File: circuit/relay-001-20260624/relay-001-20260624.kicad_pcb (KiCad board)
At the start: 2 copper layers, 169 x 126.3 mm, 15 parts, among them J1 Conn_01x03_Pin, J10 Conn_01x02_Pin, J11 Conn_01x02_Pin, J12 Conn_01x02_Pin, J13 Conn_01x02_Pin, J14 Conn_01x02_Pin, J15 Conn_01x02_Pin, J2 Conn_02x05_Odd_Even, J3 Conn_02x08_Odd_Even, J4 Conn_02x09_Odd_Even, J5 Conn_01x02_Pin, J6 Conn_01x02_Pin, J7 Conn_01x02_Pin, J8 Conn_01x02_Pin, J9 Conn_01x02_Pin

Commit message: Update 供給基板のボード図を進めた
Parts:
- moved J14 184.3 mm to (185.2, 35.6), turned to -34.8 degrees
- moved J13 171.7 mm to (202.6, 123.8), turned to -124.8 degrees
- moved J9 146.4 mm to (177.4, 104.2), turned to -90 degrees
- moved J11 111.6 mm to (112.6, 37.0), turned to 34.8 degrees
- moved J7 86.1 mm to (121.4, 90.4), turned to 90 degrees
- moved J6 74.9 mm to (114.8, 103.4), turned to 90 degrees
- moved J1 71.9 mm to (123.8, 98.9)
- moved J15 69.6 mm to (80.3, 95.2), turned to -90 degrees
- moved J12 67.6 mm to (98.4, 125.7), turned to 124.8 degrees
- moved J8 51.6 mm to (186.3, 107.9)
- moved J4 16.8 mm to (205.0, 76.1), turned to -90 degrees
- moved J5 8.42 mm to (114.8, 77.4)
- moved J10 3.67 mm to (135.8, 119.0)
- moved J2 3.67 mm to (144.8, 62.7)
- moved J3 3.67 mm to (150.3, 119.4)
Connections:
- J10 pad 1: VCC -> GND
- J10 pad 2: GND -> VCC
- J2 pad 1: GND -> EN_{Boost}
- J2 pad 10: +3.3V -> GND
- J2 pad 2: EN_{Boost} -> GND
- J2 pad 3: EN_{Dribbler-Front} -> Kick_{Chip}
- J2 pad 4: Kick_{Chip} -> EN_{Dribbler-Front}
- J2 pad 5: PH_{Dribbler-Front} -> VCC
- J2 pad 6: VCC -> PH_{Dribbler-Front}
- J2 pad 7: BallCatch_{Front} -> Kick_{Stroke}
- J2 pad 8: Kick_{Stroke} -> BallCatch_{Front}
- J2 pad 9: GND -> +3.3V
- J3 pad 1: Motor_{OUT1-1} -> BallCatch_{Back}
- J3 pad 10: Motor2_{PWM} -> Motor_{OUT2-2}
- J3 pad 11: Motor_{OUT3-2} -> Motor_{EN}
- J3 pad 12: Motor3_{PWM} -> Motor_{OUT2-1}
- J3 pad 13: Motor_{OUT4-1} -> +3.3V
- J3 pad 14: Motor4_{PWM} -> Motor_{OUT1-2}
- J3 pad 15: Motor_{OUT4-2} -> GND
- J3 pad 16: BallCatch_{Back} -> Motor_{OUT1-1}
- J3 pad 2: +3.3V -> Motor_{OUT4-2}
- J3 pad 3: Motor_{OUT1-2} -> Motor4_{PWM}
- J3 pad 4: GND -> Motor_{OUT4-1}
- J3 pad 5: Motor_{OUT2-1} -> Motor3_{PWM}
- J3 pad 6: Motor_{EN} -> Motor_{OUT3-2}
- J3 pad 7: Motor_{OUT2-2} -> Motor2_{PWM}
- J3 pad 8: Motor1_{PWM} -> Motor_{OUT3-1}
- J3 pad 9: Motor_{OUT3-1} -> Motor1_{PWM}
- J5 pad 1: +5V_{Line} -> GND
- J5 pad 2: GND -> +5V_{Line}
- J6 pad 1: VCC -> GND
- J6 pad 2: GND -> VCC
- J7 pad 1: +5V -> +3.3V
- J7 pad 2: +3.3V -> +5V
- J8 pad 1: +5V_{Line} -> GND
- J8 pad 2: GND -> +5V_{Line}
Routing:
- net +3.3V: track 0.00 -> 199.4 mm, vias 0 -> 1
- net VCC: track 0.00 -> 182.2 mm
- net Motor_{OUT1-2}: track 0.00 -> 139.2 mm, vias 0 -> 2
- net Motor_{OUT1-1}: track 0.00 -> 129.6 mm, vias 0 -> 2
- net Motor_{OUT4-1}: track 0.00 -> 117.5 mm, vias 0 -> 1
- net Motor3_{PWM}: track 0.00 -> 117.1 mm, vias 0 -> 1
- net Motor2_{PWM}: track 0.00 -> 113.9 mm
- net Motor1_{PWM}: track 0.00 -> 110.5 mm
- net Motor_{EN}: track 0.00 -> 108.4 mm
- net Motor_{OUT4-2}: track 0.00 -> 107.8 mm, vias 0 -> 1
- net +5V_{Line}: track 0.00 -> 88.7 mm
- net +5V: track 0.00 -> 78.0 mm
- net Motor_{OUT2-1}: track 0.00 -> 72.5 mm
- net Motor_{OUT2-2}: track 0.00 -> 70.5 mm
- net Motor_{OUT3-2}: track 0.00 -> 53.0 mm
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- added copper zone on F.Cu, net VCC
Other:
- outline, holes or cut-outs redrawn

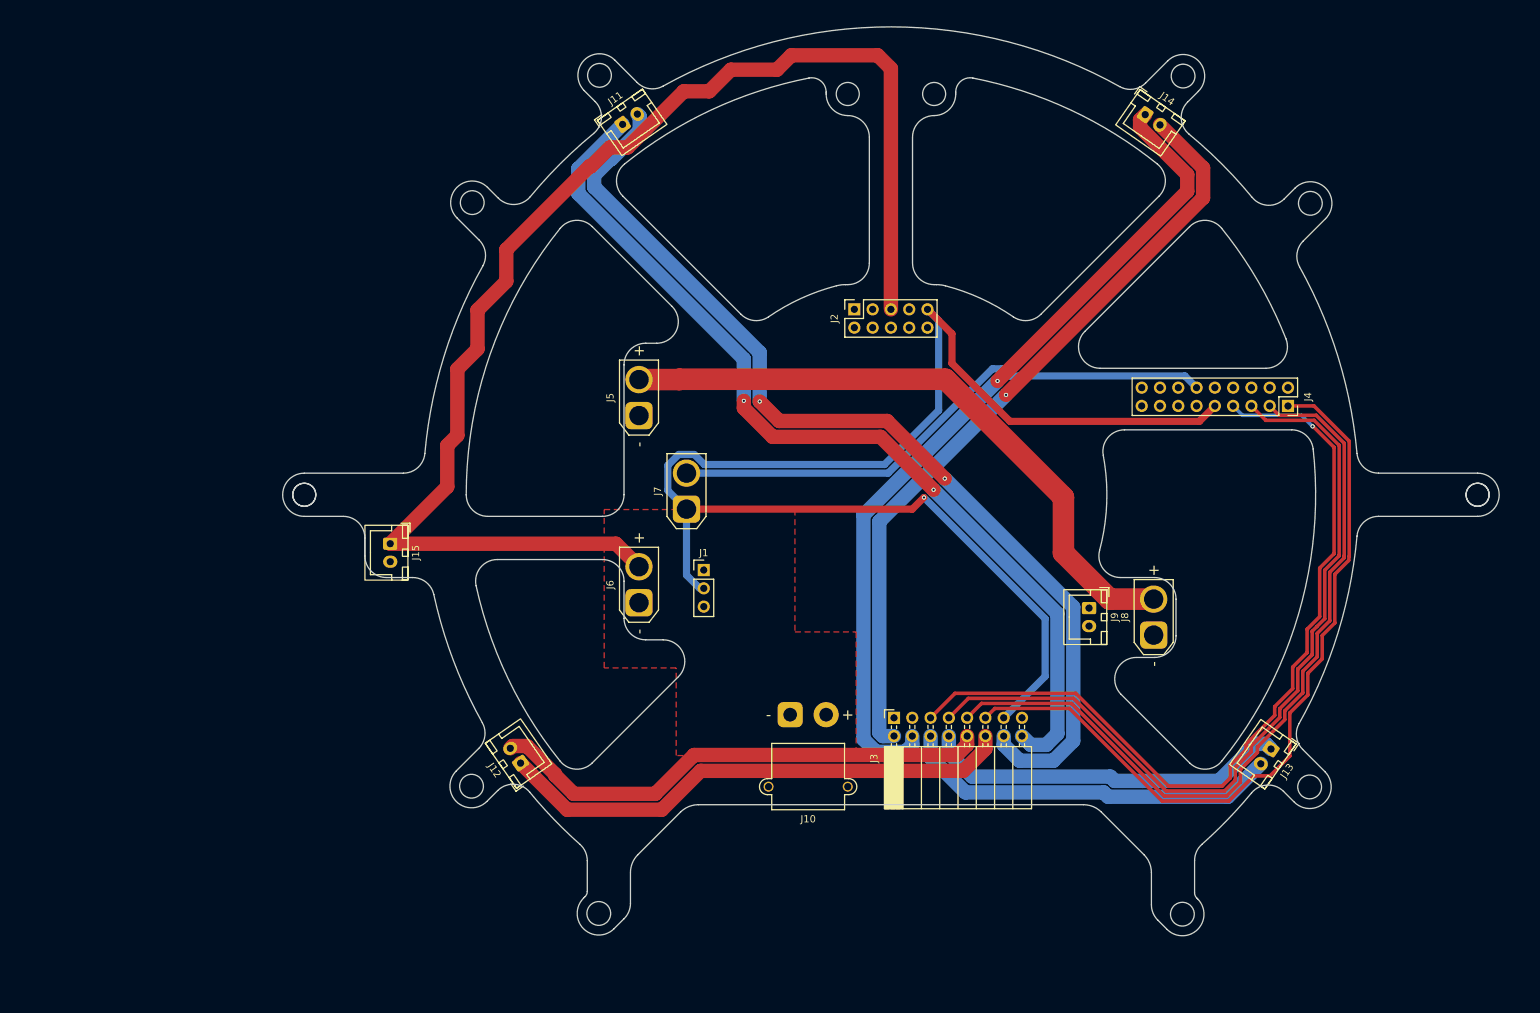
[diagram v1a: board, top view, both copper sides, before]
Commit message: Update 供給基板のDXFとボード図を更新
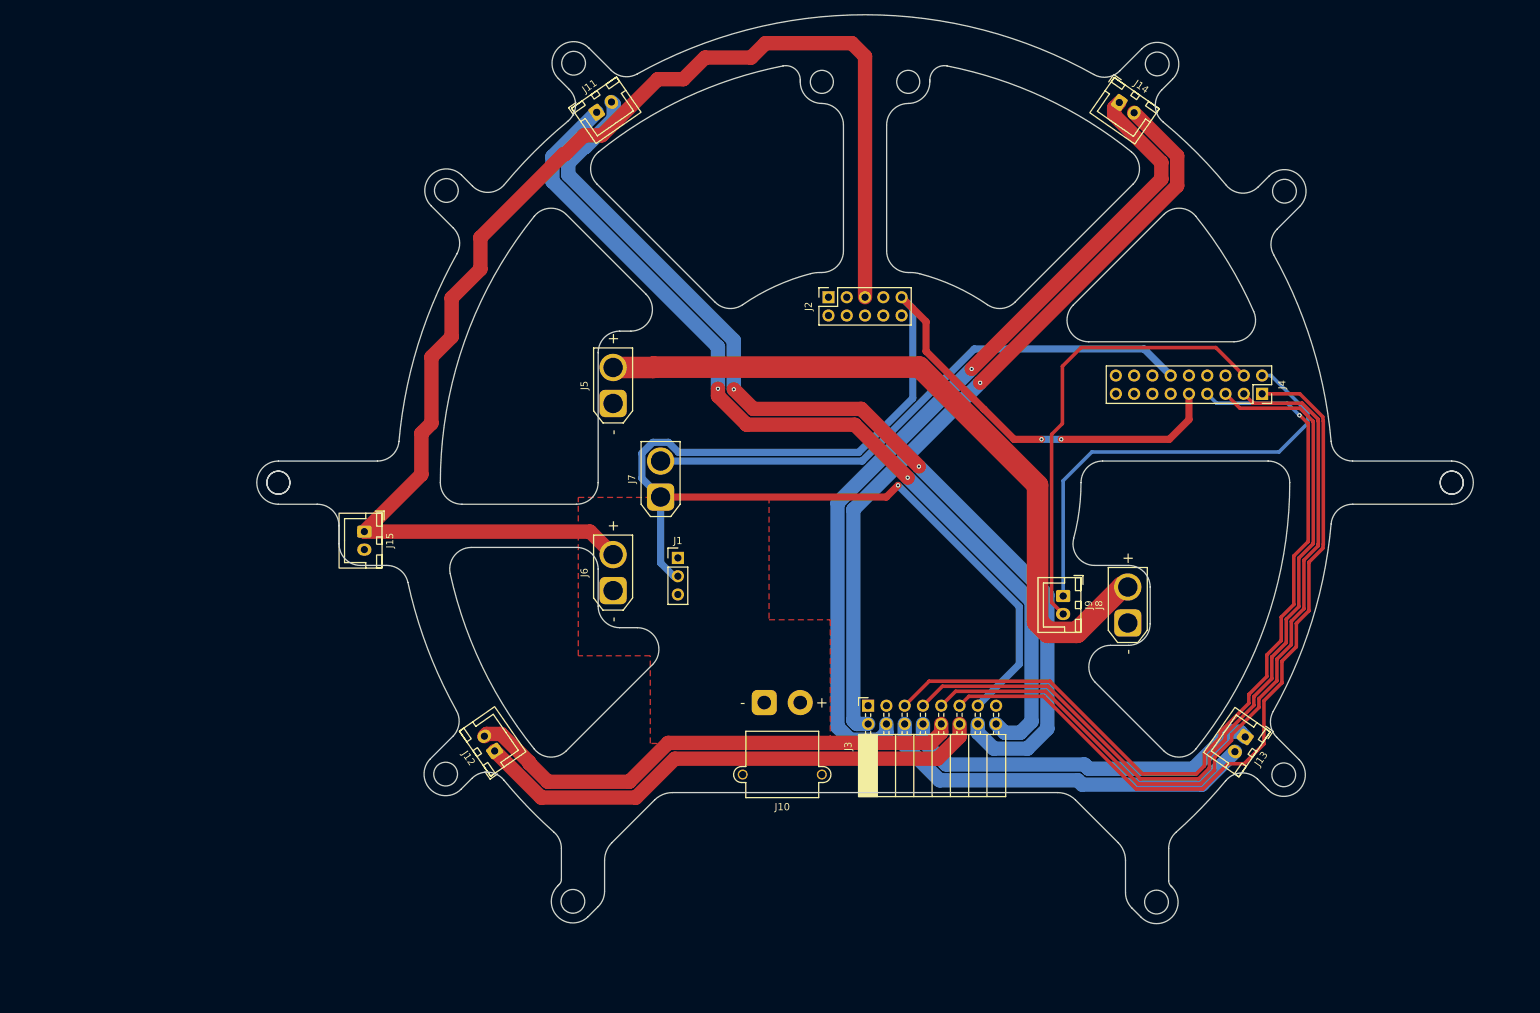
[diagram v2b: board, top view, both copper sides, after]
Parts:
- moved J1 3.97 mm to (120.2, 97.2)
- moved J3 3.97 mm to (146.7, 117.7)
- moved J5 3.97 mm to (111.2, 75.8)
- moved J6 3.97 mm to (111.2, 101.8)
- moved J2 3.97 mm to (141.2, 61.0)
- moved J10 3.97 mm to (132.2, 117.3)
- moved J12 3.97 mm to (94.8, 124.0)
- moved J13 3.97 mm to (199.0, 122.1)
- moved J14 3.97 mm to (181.6, 34.0)
- moved J15 3.97 mm to (76.7, 93.6)
- moved J9 3.97 mm to (173.8, 102.5)
- moved J11 3.97 mm to (109.0, 35.3)
- moved J7 3.97 mm to (117.8, 88.8)
- moved J4 3.97 mm to (201.4, 74.4)
- moved J8 3.97 mm to (182.7, 106.3)
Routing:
- net RX_{teensy}-TX_{Arduino}-5V: track 0.00 -> 63.6 mm
- net TX_{teensy}-RX_{Arduino}-5V: track 0.00 -> 63.3 mm
- net +5V_{Line}: track 88.7 -> 100.5 mm
- net +3.3V: track 199.4 -> 205.0 mm, vias 1 -> 3
- net Motor1_{PWM}: track 110.5 -> 111.4 mm
- net Motor3_{PWM}: track 117.1 -> 118.1 mm
- net Motor2_{PWM}: track 113.9 -> 114.8 mm
- net Motor_{EN}: track 108.4 -> 109.3 mm
- net +5V: track 78.0 -> 78.8 mm
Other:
- outline, holes or cut-outs redrawn

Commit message: Update 供給基板のボード図を更新
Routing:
- net BallCatch_{Front}: track 0.00 -> 53.2 mm, vias 0 -> 3
- net +3.3V: track 205.0 -> 198.6 mm, vias 3 -> 4

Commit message: Update 供給基板のボード図を更新
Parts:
- moved J8 13.3 mm to (172.3, 114.5)
- moved J7 13.3 mm to (107.4, 97.0)
- moved J11 13.3 mm to (98.5, 43.6)
- moved J1 13.3 mm to (109.8, 105.5)
- moved J10 13.3 mm to (121.8, 125.6)
- moved J12 13.3 mm to (84.3, 132.3)
- moved J3 13.3 mm to (136.2, 126.0)
- moved J4 13.3 mm to (190.9, 82.7)
- moved J5 13.3 mm to (100.8, 84.0)
- moved J6 13.3 mm to (100.8, 110.0)
- moved J9 13.3 mm to (163.3, 110.8)
- moved J14 13.3 mm to (171.1, 42.2)
- moved J2 13.3 mm to (130.7, 69.3)
- moved J15 13.3 mm to (66.2, 101.8)
- moved J13 13.3 mm to (188.6, 130.4)
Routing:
- net BallCatch_{Back}: track 0.00 -> 88.2 mm, vias 0 -> 4
- net Motor4_{PWM}: track 0.00 -> 84.7 mm, vias 0 -> 4
- net Dribbler_{Back}: track 0.00 -> 77.3 mm, vias 0 -> 2
- net EN_{Dribbler-Front}: track 0.00 -> 56.7 mm, vias 0 -> 1
- net PH_{Dribbler-Front}: track 0.00 -> 56.7 mm, vias 0 -> 1
- net EN_{Boost}: track 0.00 -> 56.0 mm, vias 0 -> 1
- net Kick_{Chip}: track 0.00 -> 46.4 mm, vias 0 -> 1
- net Kick_{Stroke}: track 0.00 -> 41.5 mm, vias 0 -> 1
- net +5V: track 78.8 -> 83.4 mm
- net BallCatch_{Front}: track 53.2 -> 54.6 mm
- net RX_{teensy}-TX_{Arduino}-5V: track 63.6 -> 64.7 mm
- added copper zone on F.Cu, net GND

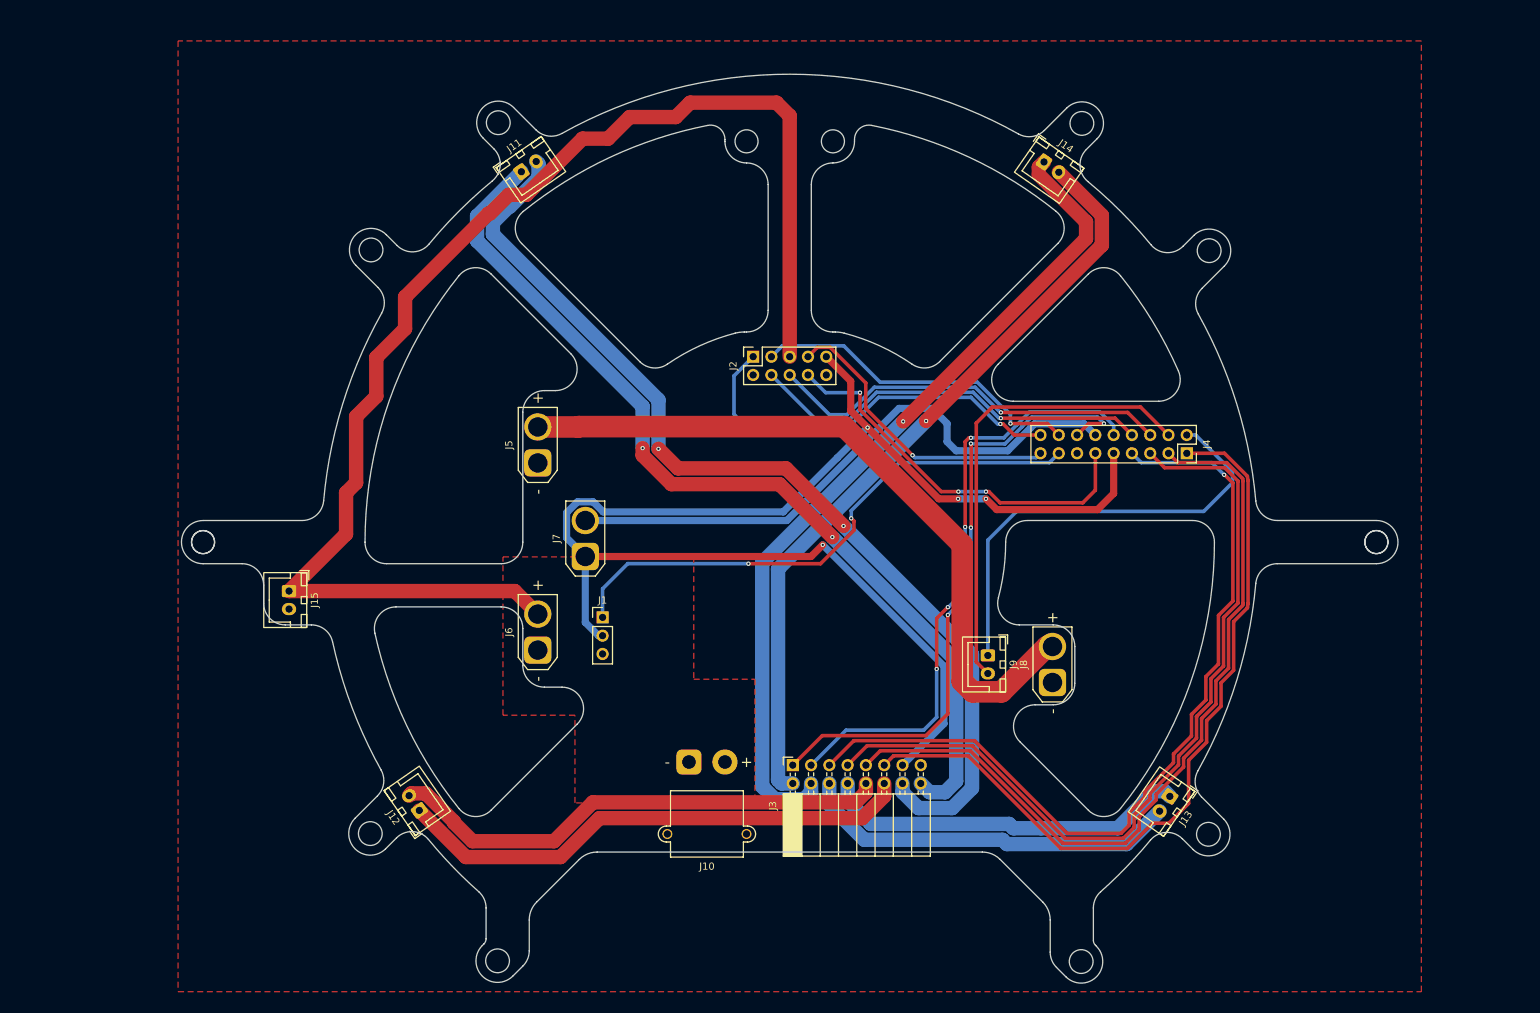
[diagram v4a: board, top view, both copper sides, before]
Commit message: Update 供給基板のボード図、キッカー基板の発注ファイルを更新
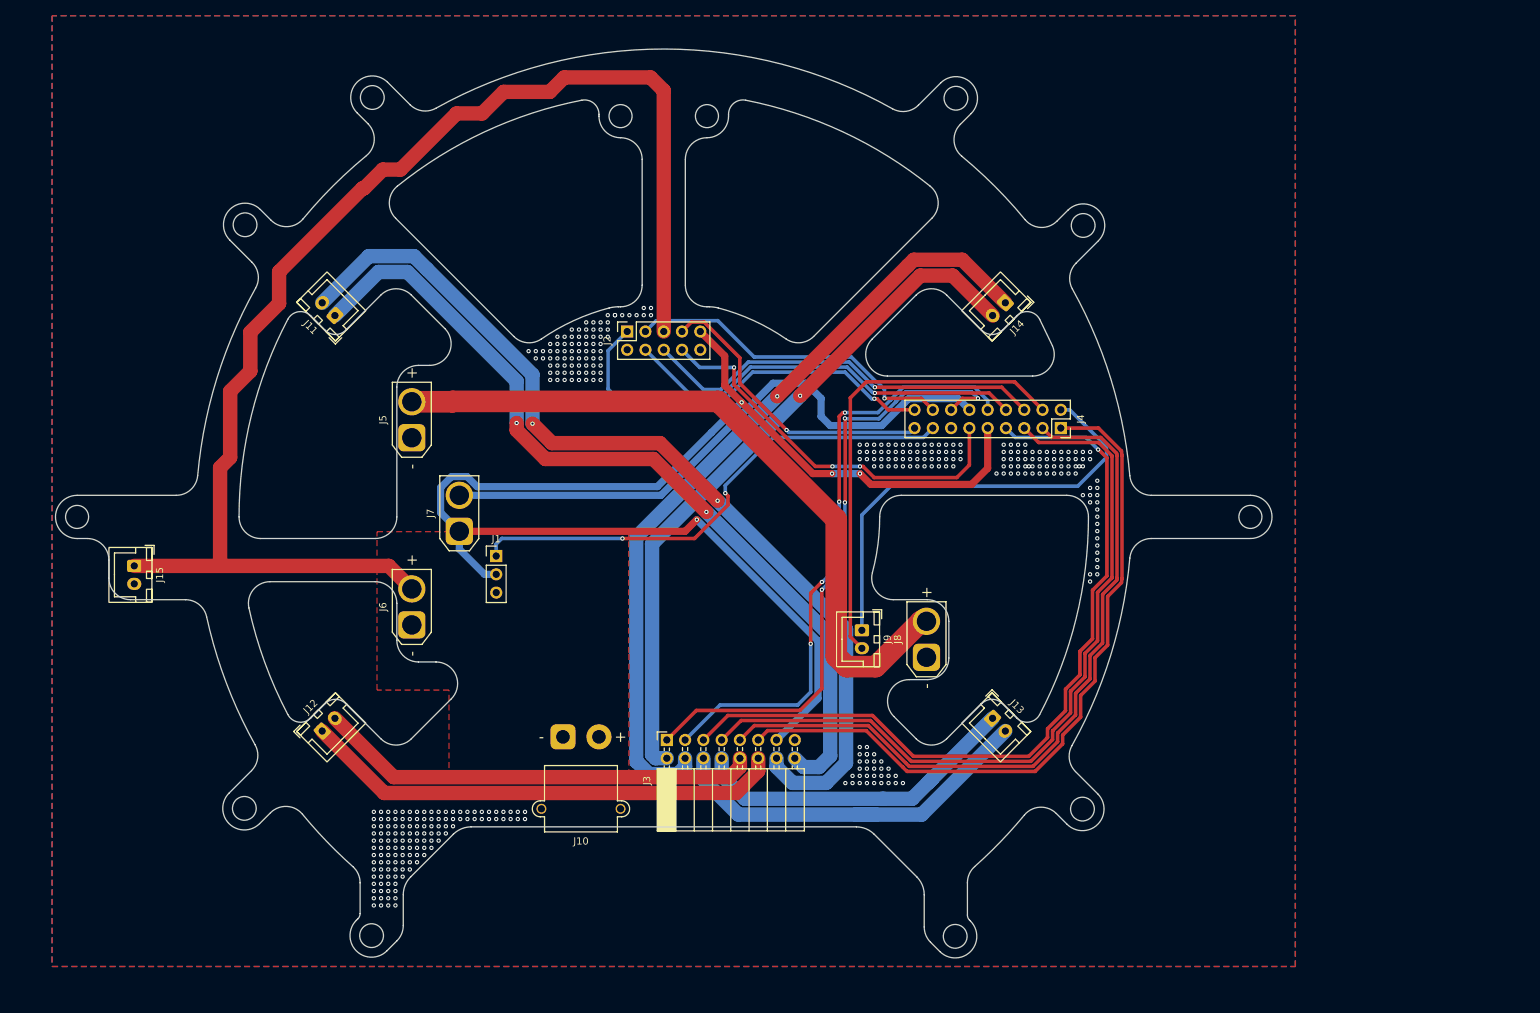
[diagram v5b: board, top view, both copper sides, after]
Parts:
- moved J11 32.7 mm to (72.6, 63.5), turned to 135 degrees
- moved J13 26.9 mm to (164.0, 119.5), turned to -45 degrees
- moved J15 21.8 mm to (44.7, 98.3)
- moved J14 20.3 mm to (165.7, 61.8), turned to -135 degrees
- moved J2 17.8 mm to (113.2, 65.8)
- moved J10 17.8 mm to (104.3, 122.1)
- moved J3 17.8 mm to (118.7, 122.5)
- moved J4 17.8 mm to (173.4, 79.2)
- moved J5 17.8 mm to (83.3, 80.5)
- moved J6 17.8 mm to (83.3, 106.5)
- moved J7 17.8 mm to (89.9, 93.5)
- moved J8 17.8 mm to (154.8, 111.0)
- moved J9 17.8 mm to (145.8, 107.3)
- moved J12 17.4 mm to (70.8, 121.3), turned to 45 degrees
- moved J1 17.1 mm to (95.0, 97.0)
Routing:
- net Motor_{OUT4-2}: track 107.8 -> 96.6 mm
- net Motor_{OUT1-1}: track 129.6 -> 119.0 mm
- net Motor_{OUT2-2}: track 70.5 -> 61.4 mm
- net Motor_{EN}: track 109.3 -> 100.6 mm
- net Motor_{OUT4-1}: track 117.5 -> 110.0 mm
- net Motor2_{PWM}: track 114.8 -> 107.4 mm
- net Motor1_{PWM}: track 111.4 -> 104.0 mm
- net Motor3_{PWM}: track 118.1 -> 110.7 mm
- net Motor_{OUT1-2}: track 139.2 -> 132.4 mm
- net Dribbler_{Back}: track 77.3 -> 71.1 mm
- net Motor_{OUT3-1}: track 52.9 -> 46.9 mm
- net Motor_{OUT2-1}: track 72.5 -> 67.2 mm
- net +3.3V: track 198.6 -> 195.3 mm
- net Motor_{OUT3-2}: track 53.0 -> 54.6 mm
- net VCC: track 182.2 -> 183.0 mm
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- added copper zone on B.Cu, net GND
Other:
- outline, holes or cut-outs redrawn

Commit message: Update 供給基板の3DファイルとPCBを出力
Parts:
- moved J1 4.61 mm to (98.0, 93.5)
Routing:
- net Dribbler_{Back}: track 71.1 -> 66.6 mm
- net +3.3V: track 195.3 -> 197.0 mm
- net GND: vias 373 -> 1699

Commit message: Update 供給基板のPCBが完成した
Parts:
- moved J9 56.7 mm to (90.5, 119.8), turned to 45 degrees
- moved J1 14.2 mm to (111.5, 98.0)
- moved J10 14.2 mm to (117.8, 126.6)
- moved J11 14.2 mm to (86.1, 68.0)
- moved J12 14.2 mm to (84.3, 125.8)
- moved J13 14.2 mm to (177.5, 124.0)
- moved J15 14.2 mm to (58.2, 102.8)
- moved J2 14.2 mm to (126.7, 70.3)
- moved J3 14.2 mm to (132.2, 127.0)
- moved J4 14.2 mm to (186.9, 83.7)
- moved J5 14.2 mm to (96.8, 85.0)
- moved J6 14.2 mm to (96.8, 111.0)
- moved J7 14.2 mm to (103.4, 98.0)
- moved J8 14.2 mm to (168.3, 115.5)
- moved J14 14.2 mm to (179.2, 66.3)
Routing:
- net RX_{teensy}-TX_{Arduino}-5V: track 64.7 -> 133.0 mm, vias 0 -> 2
- net TX_{teensy}-RX_{Arduino}-5V: track 63.3 -> 130.8 mm, vias 0 -> 2
- net Dribbler_{Back}: track 66.6 -> 75.3 mm, vias 2 -> 1
- net PH_{Dribbler-Front}: track 56.7 -> 54.8 mm
- net EN_{Dribbler-Front}: track 56.7 -> 54.8 mm
- net GND: vias 1699 -> 2549
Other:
- outline, holes or cut-outs redrawn
